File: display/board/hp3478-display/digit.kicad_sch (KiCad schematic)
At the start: 14 parts

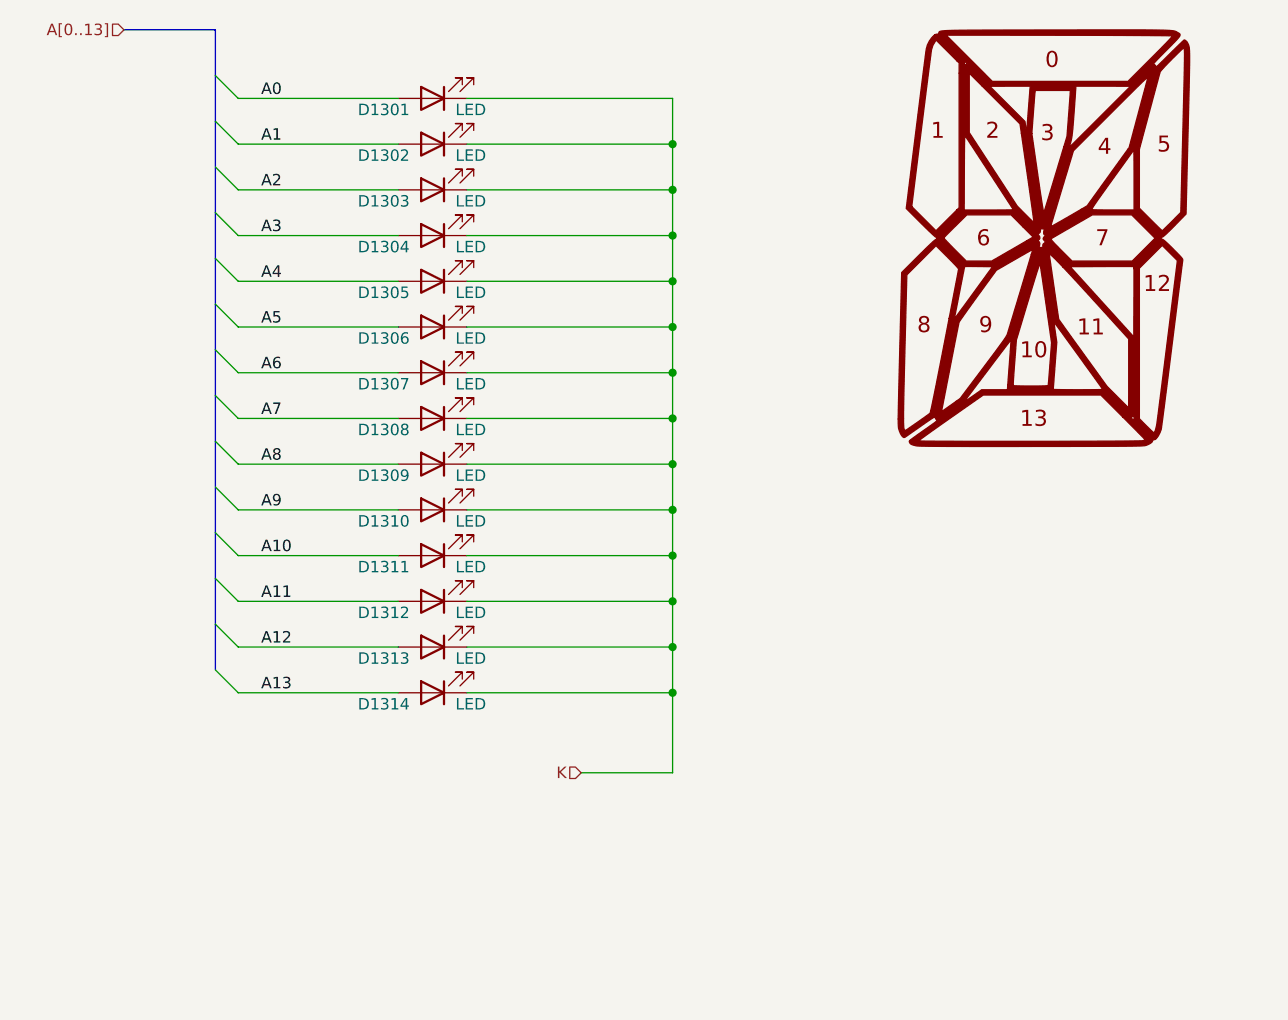
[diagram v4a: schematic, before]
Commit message: Improve workflow for getting digit shapes into KiCAD.
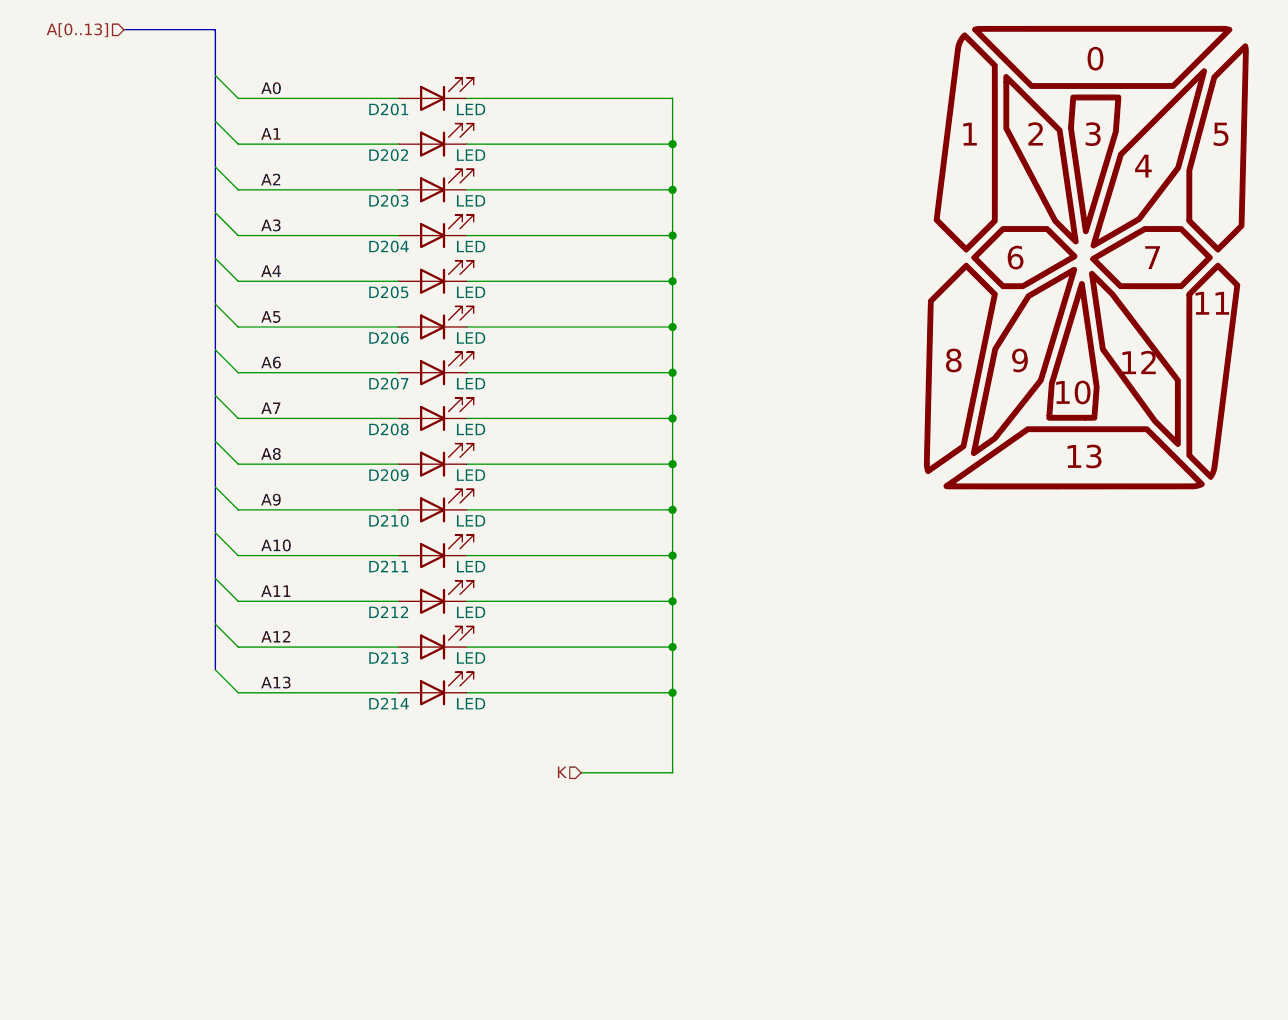
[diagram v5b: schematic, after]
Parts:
- renumbered D1301 to D201, D1302 to D202, D1303 to D203, D1304 to D204, D1305 to D205, D1306 to D206, D1307 to D207, D1308 to D208, D1309 to D209, D1310 to D210, D1311 to D211, D1312 to D212, D1313 to D213, D1314 to D214
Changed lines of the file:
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@@
     (effects (font (size 1.27 1.27)) (justify right))
   )
-  (symbol (lib_id "Device:LED") (at 74.93 88.9 180)
-    (in_bom yes) (on_board yes)
-    (property "Reference" "D1307" (id 0) (at 72.39 90.17 0)
+  (symbol (lib_id "Device:LED") (at 74.93 88.9 180) (unit 1)
+    (in_bom yes) (on_board yes)
+    (property "Reference" "D207" (id 0) (at 72.39 90.17 0)
       (effects (font (size 1.27 1.27)) (justify left))
     )
@@
     (pin "2")
   )
-  (symbol (lib_id "Device:LED") (at 74.93 68.58 180)
-    (in_bom yes) (on_board yes)
-    (property "Reference" "D1303" (id 0) (at 72.39 69.85 0)
+  (symbol (lib_id "Device:LED") (at 74.93 68.58 180) (unit 1)
+    (in_bom yes) (on_board yes)
+    (property "Reference" "D203" (id 0) (at 72.39 69.85 0)
       (effects (font (size 1.27 1.27)) (justify left))
     )
@@
     (pin "2")
   )
-  (symbol (lib_id "Device:LED") (at 74.93 93.98 180)
-    (in_bom yes) (on_board yes)
-    (property "Reference" "D1308" (id 0) (at 72.39 95.25 0)
+  (symbol (lib_id "Device:LED") (at 74.93 93.98 180) (unit 1)
+    (in_bom yes) (on_board yes)
+    (property "Reference" "D208" (id 0) (at 72.39 95.25 0)
       (effects (font (size 1.27 1.27)) (justify left))
     )
@@
     (pin "2")
   )
-  (symbol (lib_id "0Local:Digit_Legend_Large") (at 147.32 76.2 0)
+  (symbol (lib_id "0Local:Digit_Legend_S5.0") (at 147.32 76.2 0) (unit 1)
     (in_bom no) (on_board no)
-    (property "Reference" "#G1301" (id 0) (at 147.32 51.435 0)
+    (property "Reference" "#G201" (id 0) (at 147.32 51.435 0)
       (effects (font (size 1.27 1.27)) hide)
     )
@@
     )
   )
-  (symbol (lib_id "Device:LED") (at 74.93 104.14 180)
-    (in_bom yes) (on_board yes)
-    (property "Reference" "D1310" (id 0) (at 72.39 105.41 0)
+  (symbol (lib_id "Device:LED") (at 74.93 104.14 180) (unit 1)
+    (in_bom yes) (on_board yes)
+    (property "Reference" "D210" (id 0) (at 72.39 105.41 0)
       (effects (font (size 1.27 1.27)) (justify left))
     )
@@
     (pin "2")
   )
-  (symbol (lib_id "Device:LED") (at 74.93 73.66 180)
-    (in_bom yes) (on_board yes)
-    (property "Reference" "D1304" (id 0) (at 72.39 74.93 0)
+  (symbol (lib_id "Device:LED") (at 74.93 73.66 180) (unit 1)
+    (in_bom yes) (on_board yes)
+    (property "Reference" "D204" (id 0) (at 72.39 74.93 0)
       (effects (font (size 1.27 1.27)) (justify left))
     )
@@
     (pin "2")
   )
-  (symbol (lib_id "Device:LED") (at 74.93 119.38 180)
-    (in_bom yes) (on_board yes)
-    (property "Reference" "D1313" (id 0) (at 72.39 120.65 0)
+  (symbol (lib_id "Device:LED") (at 74.93 119.38 180) (unit 1)
+    (in_bom yes) (on_board yes)
+    (property "Reference" "D213" (id 0) (at 72.39 120.65 0)
       (effects (font (size 1.27 1.27)) (justify left))
     )
@@
     (pin "2")
   )
-  (symbol (lib_id "Device:LED") (at 74.93 124.46 180)
-    (in_bom yes) (on_board yes)
-    (property "Reference" "D1314" (id 0) (at 72.39 125.73 0)
+  (symbol (lib_id "Device:LED") (at 74.93 124.46 180) (unit 1)
+    (in_bom yes) (on_board yes)
+    (property "Reference" "D214" (id 0) (at 72.39 125.73 0)
       (effects (font (size 1.27 1.27)) (justify left))
     )
@@
     (pin "2")
   )
-  (symbol (lib_id "Device:LED") (at 74.93 114.3 180)
-    (in_bom yes) (on_board yes)
-    (property "Reference" "D1312" (id 0) (at 72.39 115.57 0)
+  (symbol (lib_id "Device:LED") (at 74.93 114.3 180) (unit 1)
+    (in_bom yes) (on_board yes)
+    (property "Reference" "D212" (id 0) (at 72.39 115.57 0)
       (effects (font (size 1.27 1.27)) (justify left))
     )
@@
     (pin "2")
   )
-  (symbol (lib_id "Device:LED") (at 74.93 58.42 180)
-    (in_bom yes) (on_board yes)
-    (property "Reference" "D1301" (id 0) (at 72.39 59.69 0)
+  (symbol (lib_id "Device:LED") (at 74.93 58.42 180) (unit 1)
+    (in_bom yes) (on_board yes)
+    (property "Reference" "D201" (id 0) (at 72.39 59.69 0)
       (effects (font (size 1.27 1.27)) (justify left))
     )
@@
     (pin "2")
   )
-  (symbol (lib_id "Device:LED") (at 74.93 83.82 180)
-    (in_bom yes) (on_board yes)
-    (property "Reference" "D1306" (id 0) (at 72.39 85.09 0)
+  (symbol (lib_id "Device:LED") (at 74.93 83.82 180) (unit 1)
+    (in_bom yes) (on_board yes)
+    (property "Reference" "D206" (id 0) (at 72.39 85.09 0)
       (effects (font (size 1.27 1.27)) (justify left))
     )
@@
     (pin "2")
   )
-  (symbol (lib_id "Device:LED") (at 74.93 109.22 180)
-    (in_bom yes) (on_board yes)
-    (property "Reference" "D1311" (id 0) (at 72.39 110.49 0)
+  (symbol (lib_id "Device:LED") (at 74.93 109.22 180) (unit 1)
+    (in_bom yes) (on_board yes)
+    (property "Reference" "D211" (id 0) (at 72.39 110.49 0)
       (effects (font (size 1.27 1.27)) (justify left))
     )
@@
     (pin "2")
   )
-  (symbol (lib_id "Device:LED") (at 74.93 78.74 180)
-    (in_bom yes) (on_board yes)
-    (property "Reference" "D1305" (id 0) (at 72.39 80.01 0)
+  (symbol (lib_id "Device:LED") (at 74.93 78.74 180) (unit 1)
+    (in_bom yes) (on_board yes)
+    (property "Reference" "D205" (id 0) (at 72.39 80.01 0)
       (effects (font (size 1.27 1.27)) (justify left))
     )
@@
     (pin "2")
   )
-  (symbol (lib_id "Device:LED") (at 74.93 99.06 180)
-    (in_bom yes) (on_board yes)
-    (property "Reference" "D1309" (id 0) (at 72.39 100.33 0)
+  (symbol (lib_id "Device:LED") (at 74.93 99.06 180) (unit 1)
+    (in_bom yes) (on_board yes)
+    (property "Reference" "D209" (id 0) (at 72.39 100.33 0)
       (effects (font (size 1.27 1.27)) (justify left))
     )
@@
     (pin "2")
   )
-  (symbol (lib_id "Device:LED") (at 74.93 63.5 180)
-    (in_bom yes) (on_board yes)
-    (property "Reference" "D1302" (id 0) (at 72.39 64.77 0)
-      (effects (font (size 1.27 1.27)) (justify left))
-    )
+  (symbol (lib_id "Device:LED") (at 74.93 63.5 180) (unit 1)
+    (in_bom yes) (on_board yes)
+    (property "Reference" "D202" (id 0) (at 72.39 64.77 0)
+      (effects (font (size 1.27 1.27)) (justify left))
+    )

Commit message: Swap anode and cathode - SM16206 is a low-side driver.
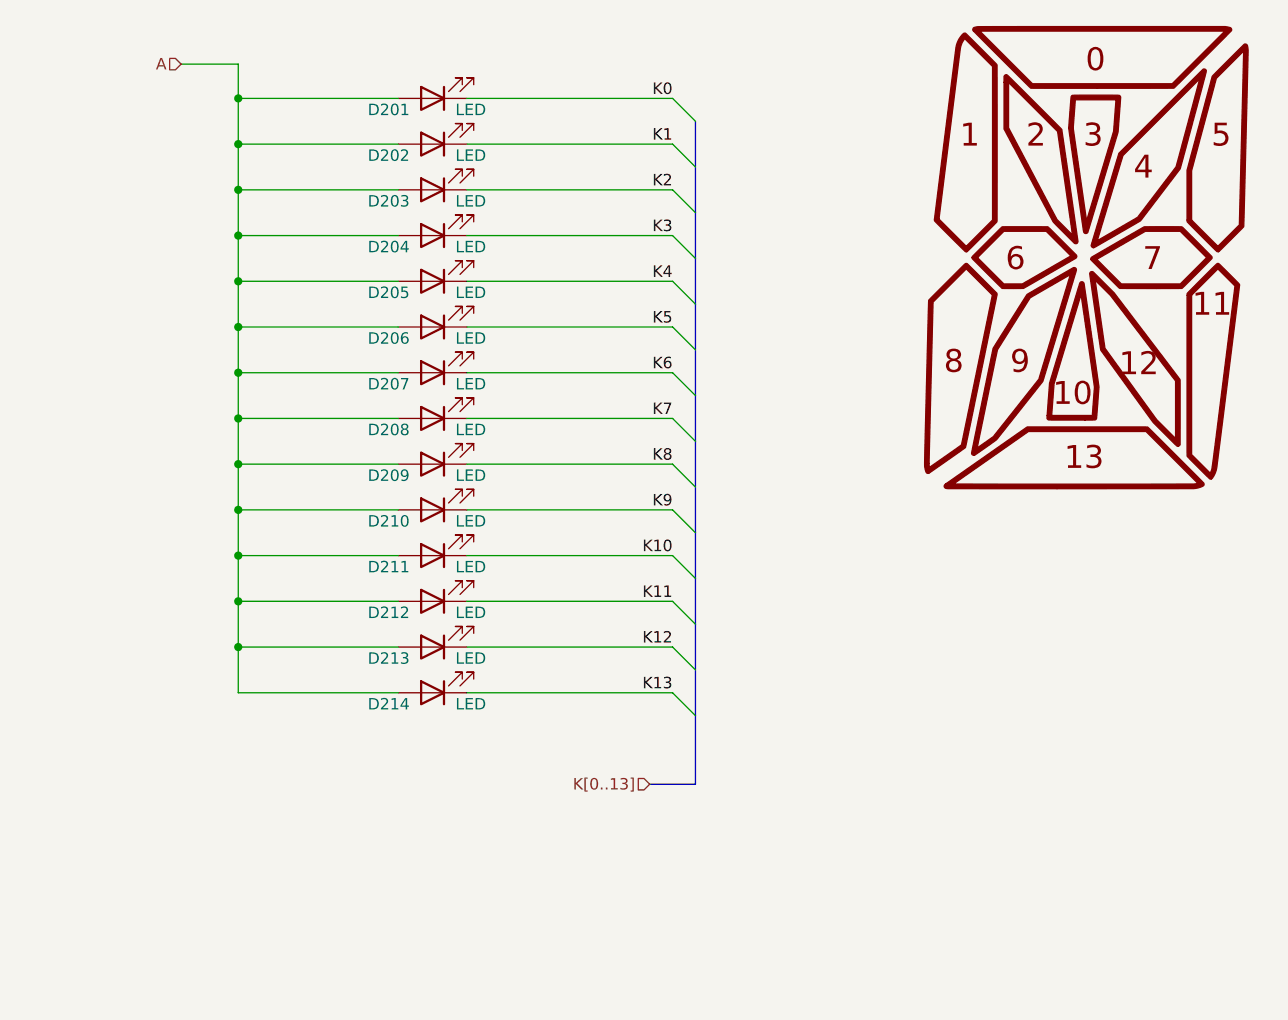
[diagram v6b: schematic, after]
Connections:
- net A1 is gone; now on net A: D202.2 (A)
- net A10 is gone; now on net A: D211.2 (A)
- net A11 is gone; now on net A: D212.2 (A)
- net A12 is gone; now on net A: D213.2 (A)
- net A13 is gone; now on net A: D214.2 (A)
- net A2 is gone; now on net A: D203.2 (A)
- net A3 is gone; now on net A: D204.2 (A)
- net A4 is gone; now on net A: D205.2 (A)
- net A5 is gone; now on net A: D206.2 (A)
- net A6 is gone; now on net A: D207.2 (A)
- net A7 is gone; now on net A: D208.2 (A)
- net A8 is gone; now on net A: D209.2 (A)
- net A9 is gone; now on net A: D210.2 (A)
- net A0 renamed A
- removed net K: D201.1 (K), D202.1 (K), D203.1 (K), D204.1 (K), D205.1 (K), D206.1 (K), D207.1 (K), D208.1 (K), D209.1 (K), D210.1 (K), D211.1 (K), D212.1 (K), D213.1 (K), D214.1 (K)
- new net K0: D201.1 (K)
- new net K1: D202.1 (K)
- new net K10: D211.1 (K)
- new net K11: D212.1 (K)
- new net K12: D213.1 (K)
- new net K13: D214.1 (K)
- new net K2: D203.1 (K)
- new net K3: D204.1 (K)
- new net K4: D205.1 (K)
- new net K5: D206.1 (K)
- new net K6: D207.1 (K)
- new net K7: D208.1 (K)
- new net K8: D209.1 (K)
- new net K9: D210.1 (K)

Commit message: Choose LEDs and set drive current.
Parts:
- D201, D202, D203, D204, D205, D206, D207, D208, D209, D210, D211, D212, D213, D214: JLC (none) -> C2852592
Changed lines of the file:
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@@
+      (effects (font (size 1.27 1.27)) hide)
+    )
+    (property "JLC" "C2852592" (id 4) (at 74.93 88.9 0)
       (effects (font (size 1.27 1.27)) hide)
     )
@@
       (effects (font (size 1.27 1.27)) hide)
     )
+    (property "JLC" "C2852592" (id 4) (at 74.93 68.58 0)
+      (effects (font (size 1.27 1.27)) hide)
+    )
     (pin "1")
     (pin "2")
@@
     )
     (property "Datasheet" "~" (id 3) (at 74.93 93.98 0)
+      (effects (font (size 1.27 1.27)) hide)
+    )
+    (property "JLC" "C2852592" (id 4) (at 74.93 93.98 0)
       (effects (font (size 1.27 1.27)) hide)
     )
@@
       (effects (font (size 1.27 1.27)) hide)
     )
+    (property "JLC" "C2852592" (id 4) (at 74.93 104.14 0)
+      (effects (font (size 1.27 1.27)) hide)
+    )
     (pin "1")
     (pin "2")
@@
       (effects (font (size 1.27 1.27)) hide)
     )
+    (property "JLC" "C2852592" (id 4) (at 74.93 73.66 0)
+      (effects (font (size 1.27 1.27)) hide)
+    )
     (pin "1")
     (pin "2")
@@
       (effects (font (size 1.27 1.27)) hide)
     )
+    (property "JLC" "C2852592" (id 4) (at 74.93 119.38 0)
+      (effects (font (size 1.27 1.27)) hide)
+    )
     (pin "1")
     (pin "2")
@@
       (effects (font (size 1.27 1.27)) hide)
     )
+    (property "JLC" "C2852592" (id 4) (at 74.93 124.46 0)
+      (effects (font (size 1.27 1.27)) hide)
+    )
     (pin "1")
     (pin "2")
@@
       (effects (font (size 1.27 1.27)) hide)
     )
+    (property "JLC" "C2852592" (id 4) (at 74.93 114.3 0)
+      (effects (font (size 1.27 1.27)) hide)
+    )
     (pin "1")
     (pin "2")
@@
       (effects (font (size 1.27 1.27)) hide)
     )
+    (property "JLC" "C2852592" (id 4) (at 74.93 58.42 0)
+      (effects (font (size 1.27 1.27)) hide)
+    )
     (pin "1")
     (pin "2")
@@
       (effects (font (size 1.27 1.27)) hide)
     )
+    (property "JLC" "C2852592" (id 4) (at 74.93 83.82 0)
+      (effects (font (size 1.27 1.27)) hide)
+    )
     (pin "1")
     (pin "2")
@@
       (effects (font (size 1.27 1.27)) hide)
     )
+    (property "JLC" "C2852592" (id 4) (at 74.93 109.22 0)
+      (effects (font (size 1.27 1.27)) hide)
+    )
     (pin "1")
     (pin "2")
@@
       (effects (font (size 1.27 1.27)) hide)
     )
+    (property "JLC" "C2852592" (id 4) (at 74.93 78.74 0)
+      (effects (font (size 1.27 1.27)) hide)
+    )
     (pin "1")
     (pin "2")
@@
       (effects (font (size 1.27 1.27)) hide)
     )
+    (property "JLC" "C2852592" (id 4) (at 74.93 99.06 0)
+      (effects (font (size 1.27 1.27)) hide)
+    )
     (pin "1")
     (pin "2")
@@
       (effects (font (size 1.27 1.27)) hide)
     )
+    (property "JLC" "C2852592" (id 4) (at 74.93 63.5 0)
+      (effects (font (size 1.27 1.27)) hide)
+    )
